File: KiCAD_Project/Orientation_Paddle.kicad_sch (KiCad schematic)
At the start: 54 parts, among them J1 NP_Conn_01x04_Relief, J2 1-0001205, J3 NP_Conn_01x03_Relief, J4 NP_Conn_01x02_Relief, J5 NP_Conn_01x02_Relief, J6 NP_Conn_01x04, J7 NP_Conn_01x04, J8 NP_Conn_01x02, U1 1-0001232, U2 1-0001471, U3 1-0000207, Y1 1-0000721

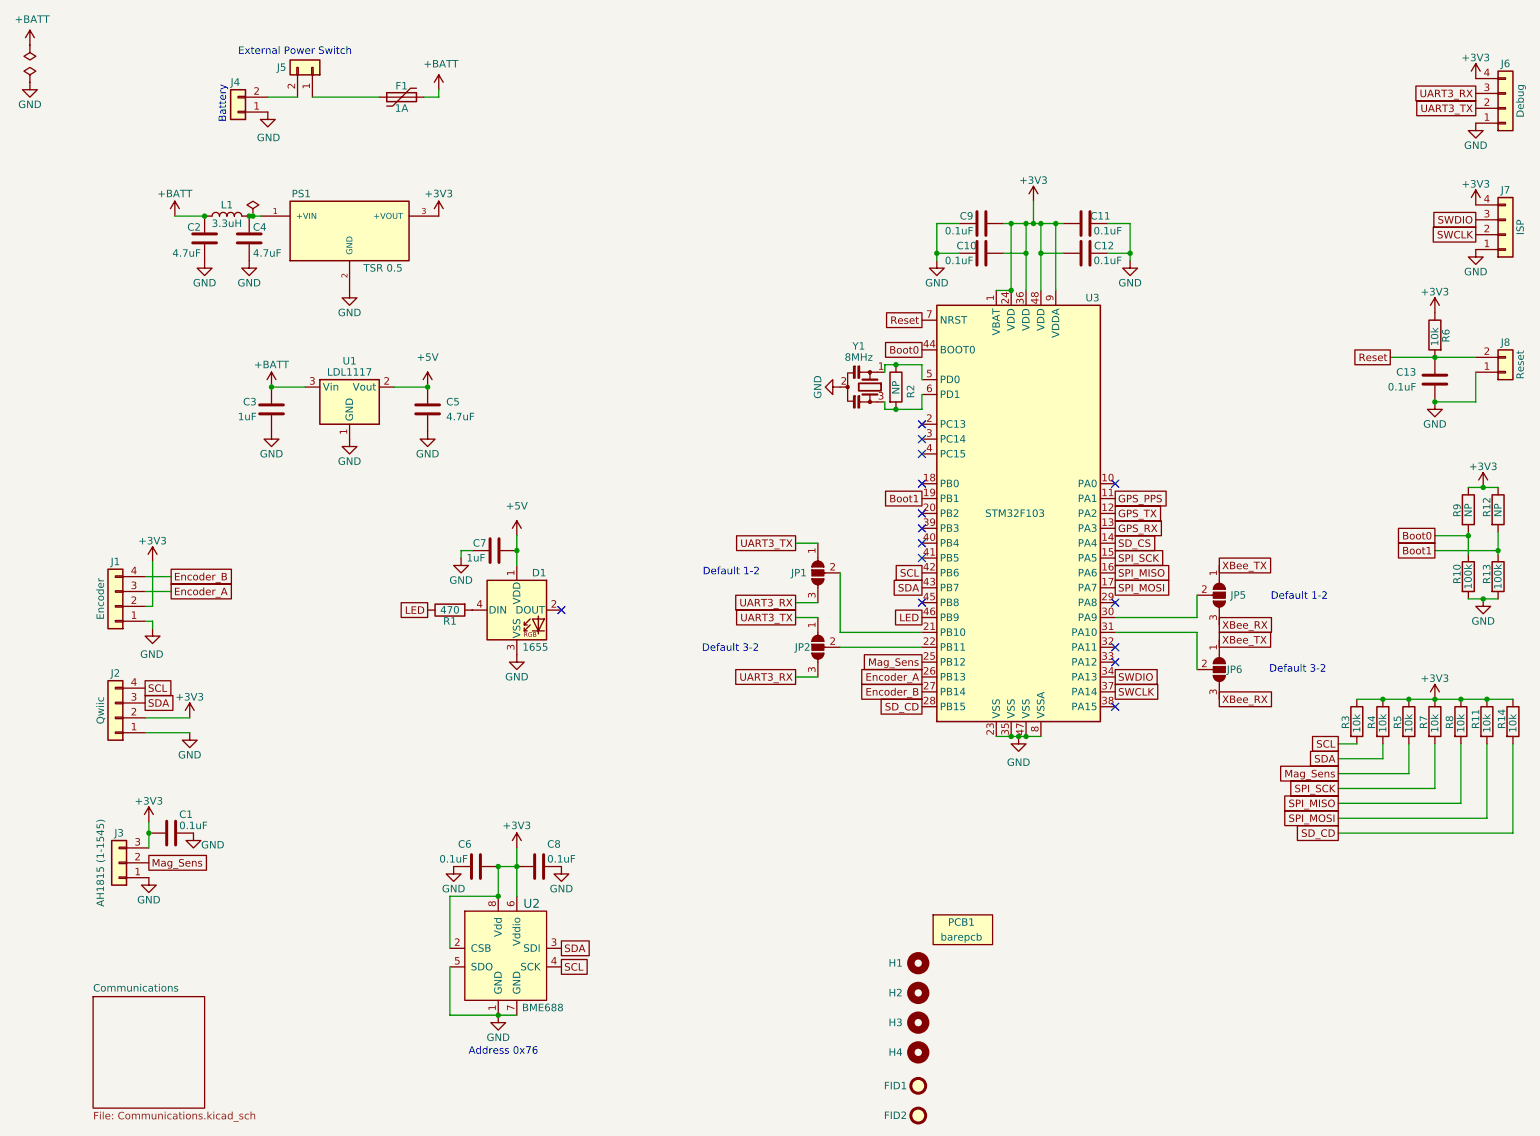
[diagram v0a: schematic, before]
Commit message: Rev 2.0 Changes: Fixed the following issues, - Issue #7 (Added RP Protection) - Issue #6 (Removed old encoder and sense connections) - Issue #5 (Solidified Serial connections by removing jumpers) - Issue #4 (Swapped GPS TX and RX) - Issue #3 (Removed old LED, add SMPL RGB LED) - Issue #2 (Labled ISCP Header) - Issue #1 (Changed DEBUG header to new SMPL DEBUG Connector) Other additions/changes: - Marked all XBEE Components as no pop - Updated board and rev numbers
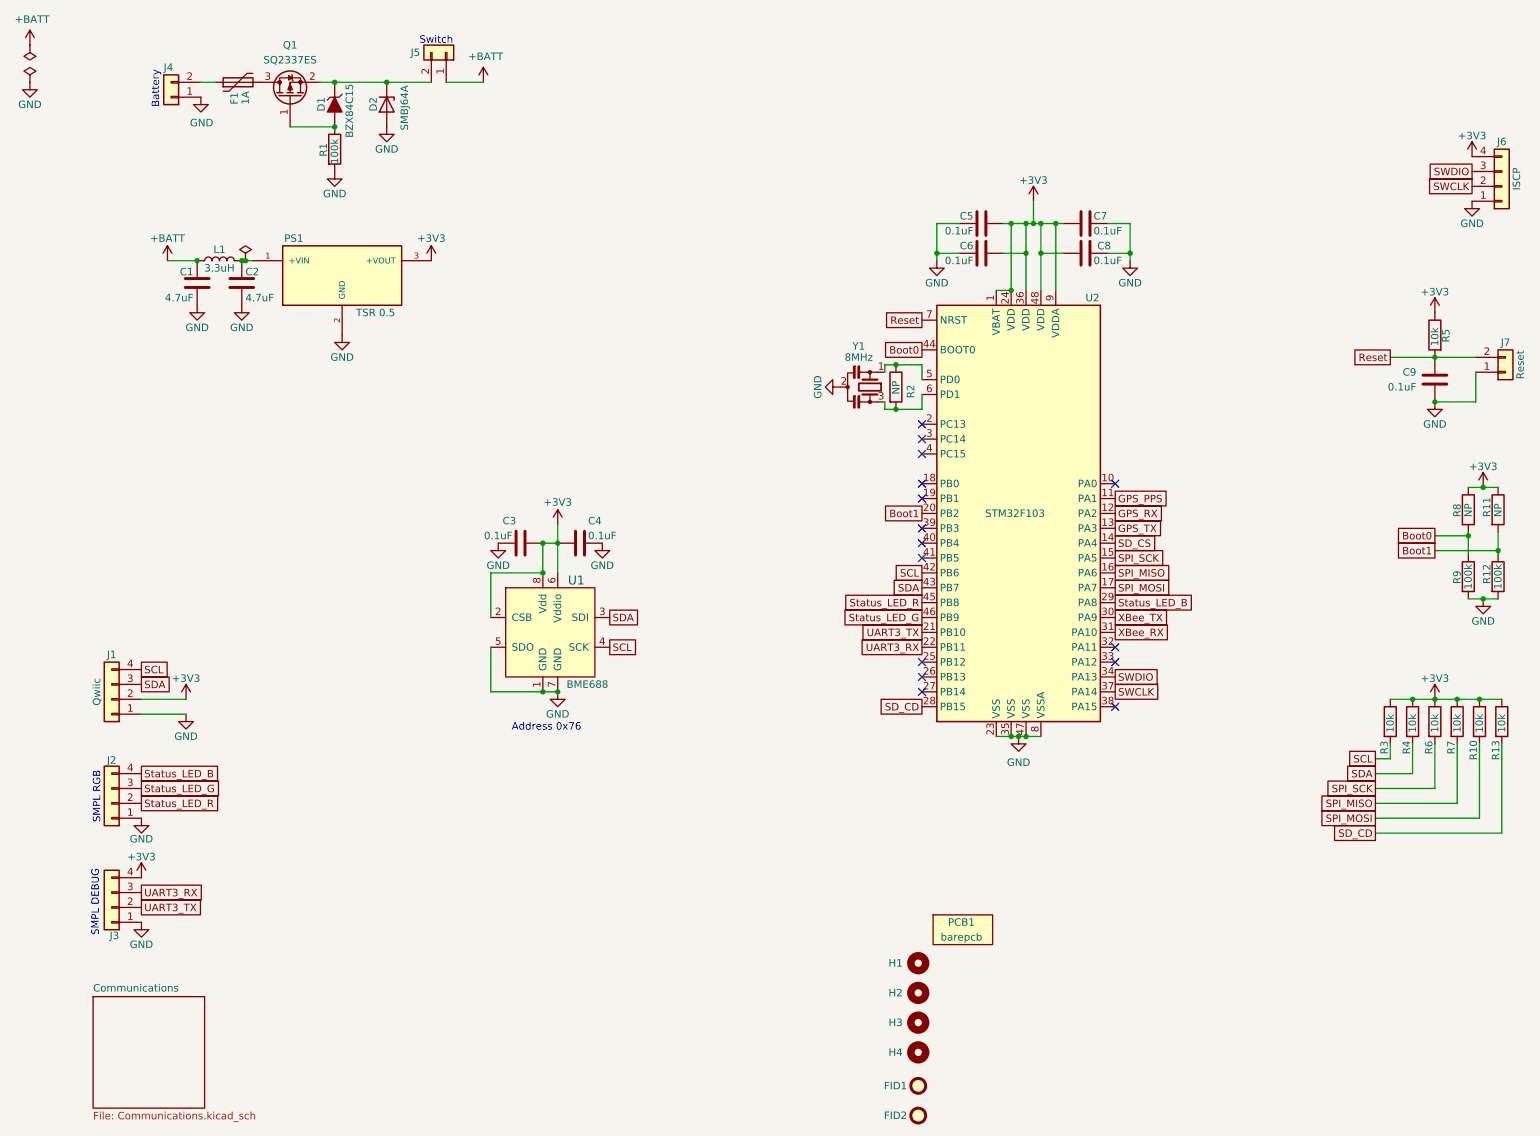
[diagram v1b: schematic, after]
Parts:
- removed C1, C6, C8: 1-0000007, capacitors_0603:1-0000007, symbol capacitors_0603:1-0000007
- removed C3, C7: 1-0000018, capacitors_0603:1-0000018, symbol capacitors_0603:1-0000018
- removed C5: 1-0000019, capacitors_0603:1-0000019, symbol capacitors_0603:1-0000019
- removed D1: 1-0000399, leds_other:1-0000399, symbol leds_other:1-0000399
- removed J1: NP_Conn_01x04_Relief, np_connectors:SolderWire_1x04_Relief, symbol np_connectors:NP_Conn_01x04_Relief
- removed J3: NP_Conn_01x03_Relief, np_connectors:SolderWire_1x03_Relief, symbol np_connectors:NP_Conn_01x03_Relief
- removed J6: NP_Conn_01x04, np_connectors:PinHeader_1x04_P2.54mm_Vertical, symbol np_connectors:NP_Conn_01x04
- removed JP1, JP2, JP5, JP6: SolderJumper_3_Open, Jumper:SolderJumper-3_P1.3mm_Open_RoundedPad1.0x1.5mm_NumberLabels, symbol Jumper:SolderJumper_3_Open
- removed R1: 1-0000679, resistors_0603:1-0000679, symbol resistors_0603:1-0000679
- removed R5: 1-0000010, resistors_0603:1-0000010, symbol resistors_0603:1-0000010
- removed U1: 1-0001232, regulators:1-0001232, symbol regulators:1-0001232
- removed U2: 1-0001471, sensors:1-0001471, symbol sensors:1-0001471
- added C3, C4: 1-0000007, capacitors_0603:1-0000007, symbol capacitors_0603:1-0000007
- added D1: 1-0001672, diodes:1-0001672, symbol diodes:1-0001672
- added D2: 1-0001537, diodes:1-0001537, symbol diodes:1-0001537
- added J2, J3: 1-0001156, connectors:1-0001156, symbol connectors:1-0001156
- added Q1: 1-0001670, mosfets:1-0001670, symbol mosfets:1-0001670
- added R1: 1-0000174, resistors_0603:1-0000174, symbol resistors_0603:1-0000174
- added U1: 1-0001471, sensors:1-0001471, symbol sensors:1-0001471
- J6: renamed from J7; PValue ISP -> ISCP
- PCB1: Internal Part Number 3-0000205 -> 3-0000267
- renumbered C2 to C1, C4 to C2, C9 to C5, C10 to C6, C11 to C7, C12 to C8, C13 to C9, J2 to J1, J8 to J7, R11 to R10, R12 to R11, R13 to R12, R14 to R13, R6 to R5, R7 to R6, R8 to R7, R9 to R8, R10 to R9, U3 to U2
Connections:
- net +3V3: now also C3.2, C4.1, J3.4 (Pin_4), U1.2 (CSB), U1.6 (Vddio), U1.8 (Vdd)
- net +BATT: now also J5.1 (Pin_1); no longer F1.2
- net Boot1: now also U2.20 (PB2); no longer U2.19 (PB1)
- net GND: now also C3.1, C4.2, D2.2 (A), J2.1 (Pin_1), J3.1 (Pin_1), R1.2, U1.1 (GND), U1.5 (SDO), U1.7 (GND)
- net GPS_RX: now also U2.12 (PA2); no longer U2.13 (PA3)
- net GPS_TX: now also U2.13 (PA3); no longer U2.12 (PA2)
- net SCL: now also U1.4 (SCK)
- net SDA: now also U1.3 (SDI)
- net UART3_RX: now also U2.22 (PB11), J3.3 (Pin_3)
- net UART3_TX: now also U2.21 (PB10), J3.2 (Pin_2)
- net XBee_RX: now also U2.31 (PA10)
- net XBee_TX: now also U2.30 (PA9)
- net at F1.1: now also J4.2 (Pin_2); no longer J5.1 (Pin_1)
- net Status_LED_B: now reaches U2.29 (PA8)
- net Status_LED_B: now also J2.4 (Pin_4)
- net Status_LED_R: now reaches U2.45 (PB8)
- net Status_LED_R: now also J2.2 (Pin_2)
- net at J5.2 (Pin_2): now also D1.3 (K), D2.1 (K), Q1.2 (S); no longer J4.2 (Pin_2)
- net Encoder_A: no longer names the net of U2.26 (PB13)
- net Encoder_B: no longer names the net of U2.27 (PB14)
- net LED renamed Status_LED_G
- net Status_LED_G: now also J2.3 (Pin_3)
- net Mag_Sens: no longer names the net of U2.25 (PB12)
- new net: F1.2, Q1.3 (D)
- new net: D1.1 (A), Q1.1 (G), R1.1
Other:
- note added: "SMPL DEBUG"
- note added: "SMPL RGB"
- note added: "Switch"
- note removed: "Default 1-2"
- note removed: "Default 3-2"
- note removed: "External Power Switch"
- moved on the sheet: C1, C2, J1, J4, J5, J6, L1, PS1, R10, R13, R3, R4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

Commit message: Make Rev 2.0 production files
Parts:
- C3, C4, U1: Populated 1 -> 0
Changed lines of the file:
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@@
 			"AAAAAAAAAAAAAAAAAAEAAAAmAAAmll+CACDQHh1QAgAAgO2YiVACAAAAAAAAAAAAAAAAAAABAAAA"
 			"AAAAAAAAAAAAAAAAAAAAAAAAAAAAAAAAAAAAAAAAAAAAAAAAAQAAAAAAAAAAAAAAAAAAAAAAAAAA"
+			"AAAAAAAAAFgBAAAAFAQAYgAAAAAAAAAyAQAA5QAAAAAAAAAAAAAAgzl9DQIAAAAAAAAAAAAAAAAA"
+			"AAAAAAAAVgEAAAAcBAA/AAAAAAAAABYBAAAvAAAAAAAAAAAAAADgYncNAgAAAAAAAAAAAAAAAAAA"
+			"AAAAAABQAQAAABQEAAYAAAAAAAAA//////////8AAAAAAAAAALAkfg0CAAAAAAAAAAAAAAAAAAAA"
+			"AAAAAGcBAAAAFAQAfAAAAAAAAAD//////////wAAAAAAAAAAgBz0AwBgAAAAAAAAAAAAAAAAAAAA"
+			"AAAAZgEAAAAUAgB9AAAAAAAAADsBAADNAAAAAAAAAAAAAADCH34NAgAAAAAAAAAAAAAAAAAAAAAA"
+			"AABlAQAAABQEAEUAAAAAAAAA/////wwBAAAAAAAAAAAAAD1Whg0CAAAAAAAAAAAAAAAAAAAAAAAA"
+			"AGIBAAAAFAQAIgAAAAAAAAD/////EQEAAAAAAAAAAAAA4GJ3DQIAAAAAAAAAAAAAAAAAAAAAAAAA"
+			"YQEAAAAUBAAGAAAAAAAAAP////8AAQAAAAAAAAAAAADgYncNAgAAAAAAAAAAAAAAAAAAAAAAAABg"
+			"AQAAABQEAAUAAAAAAAAAKgEAABoBAAAAAAAAAAAAAPxvew0CAAAAAAAAAAAAAAAAAAAAAAAAAGMB"
+			"AAAAHAQALQAAAAAAAAA8AQAAygAAAAAAAAAAAAAAwh9+DQIAAAAAAAAAAAAAAAAAAAAAAAAAZAEA"
+			"AAAUBABEAAAAAAAAABgBAAABAQAAAAAAAAAAAAD8b3sNAgAAAAAAAAAAAAAAAAAAAAAAAABdAQAA"
+			"ABwEAC0AAAAAAAAA//////////8AAAAAAAAAAGFXhg0CAAAAAAAAAAAAAAAAAAAAAAAAAHABAAAA"
+			"FAQAcwAAAAAAAAD//////////wAAAAAAAAAA/lWGDQIAAAAAAAAAAAAAAAAAAAAAAAAAbwEAAAAU"
+			"BAB0AAAAAAAAAP//////////AAAAAAAAAAClX4YNAgAAAAAAAAAAAAAAAAAAAAAAAABuAQAAABQE"
+			"AHUAAAAAAAAA//////////8AAAAAAAAAAGtfhg0CAAAAAAAAAAAAAAAAAAAAAAAAAG0BAAAAFAQA"
+			"dgAAAAAAAAD//////////wAAAAAAAAAAFVmGDQIAAAAAAAAAAAAAAAAAAAAAAAAAbAEAAAAUBAB3"
+			"AAAAAAAAAP//////////AAAAAAAAAADVWIYNAgAAAAAAAAAAAAAAAAAAAAAAAABrAQAAABQEAHgA"
+			"AAAAAAAA//////////8AAAAAAAAAALFYhg0CAAAAAAAAAAAAAAAAAAAAAAAAAGoBAAAAFAQAeQAA"
+			"AAAAAAD//wAAAAAAAAAAAAAAAAAAAAAAAAAAAAAAAAAAAAAAAAAAAAAAAAAAAAAAAAAAAAAAAAAA"
+			"AAAAAAAAAAAAAAAAAAAAAAAAAAAAAAAAAAAAAAAAAAAAAAAAAAAAAAAAAAAAAAAAAAAAAAAAAAAA"
+			"AAAAAAAAAAAAAAAAAAAAAAAAAAAAAAAAAAAAAAAAAAAAAAAAAAAAAAAAAE8UYD7oAAAAALCyNwEA"
+			"AABoCQAAAAAAAAAAAAAAAAAAAAAAAAAAAAAAAAAAAAAAAAAAAAAAAAAAAAAAAAAAAAAAAAAAAAAA"
+			"AAAAAAAAAAAAAAAAAAAAAAAAAAAAAAAAAAAAAAAAAAAAAAAAAAAAAAAAAAAAAAAAAAAAAAAAAAAA"
+			"AAAAAAAAAAAAAAAAAAAAAAAAAAAAAAAAAAAAAAAAAAAAAAAAAAAAAAAAAAAAAAAAAAAAAAAAAAAA"
+			"AAAAAAAAAAAAAAAAAAAAAAAAAAAAAAAAAAAAAAAAAAAAAAAAAAAAAAAAAAAAAAAAAAAAAAAAAAAA"
+			"AAAAAAAA/4J+gv+CfoL/gn6C/4J+gv+CfoL/gn6C/4J+gv+CfoL/gn6C/4J+gv+CfoL/gn6C/4J+"
+			"gv+CfoL/gn6C/4J+ggAAAAAAAAAAAAAAAAAAAAAAAAAAAAAAAAAAAAAAAAAA/4J+gv+CfoL/gn6C"
+			"/4J+gv+CfoL/gn6C/4J+gv+CfoL/gn6C/4J+gv+CfoL/gn6C/4J+gv+CfoL/gn6C/4J+ggAAAAAA"
+			"AAAAAAAAAAAAAAAAAAAAAAAAAAAAAAAAAAAA/4J+gv+CfoL/gn6C/4J+gv+CfoL/gn6C/4J+gv+C"
+			"foL/gn6C/4J+gv+CfoL/gn6C/4J+gv+CfoL/gn6C/4J+ggAAAAAAAAAAAAAAAAAAAAAAAAAAAAAA"
+			"AAAAAAAAAAAAAAAAAAAAAAAAAAAAAAAAAAAAAAAAAAAA/4J+gv+CfoL/gn6C/4J+ggAAAAAAAAAA"
+			"AAAAAAAAAAAAAAAAAAAAAAAAAAAAAAAAAAAAAAAAAAAAAAAAAAAAAAAAAAAAAAAAAAAAAAAAAAAA"
+			"AAAAAAAAAAAAAAAAAAAA/4J+gv+CfoL/gn6C/4J+ggAAAAAAAAAAAAAAAAAAAAAAAAAAAAAAAAAA"
+			"AAAAAAAAAAAAAAAAAAAAAAAAAAAAAAAAAAAAAAAAAAAAAAAAAAAAAAAAAAAAAAAAAAAAAAAA/4J+"
+			"gv+CfoL/gn6C/4J+ggAAAAAAAAAAAAAAAAAAAAAAAAAAAAAAAAAAAAAAAAAAAAAAAAAAAAAAAAAA"
+			"AAAAAAAAAAAAAAAAAAAAAAAAAAAAAAAAAAAAAAAAAAAAAAAA/4J+gv+CfoL/gn6C/4J+ggAAAAAA"
 			"AAAAAAAAAA=="
 		)
@@
 			)
 		)
-		(property "Populated" "1"
+		(property "Populated" "0"
 			(at 99.06 102.87 0)
 			(effects
@@
 			)
 		)
-		(property "Populated" "1"
+		(property "Populated" "0"
 			(at 93.98 118.11 0)
 			(effects
@@
 			)
 		)
-		(property "Populated" "1"
+		(property "Populated" "0"
 			(at 88.9 102.87 0)
 			(effects

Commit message: Fixed Issues #9, Issue #10 (Rev2.1)
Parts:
- PCB1: Internal Part Number 3-0000267 -> 3-0000273
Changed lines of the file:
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@@
 	(title_block
 		(title "Orientation Paddle")
-		(date "2025-06-03")
-		(rev "2.0.0")
+		(date "2025-07-03")
+		(rev "2.1.0")
 		(company "Leeman Geophysical LLC")
 		(comment 1 "(479) 373-3736")
@@
 			"gv+CfoL/gn6C/4J+ggAAAAAAAAAAAAAAAAAAAAAAAAAAAAAAAAAAAAAAAAAAAAAAAAAAAAAAAAAA"
 			"AAAAAAAAAAAAAAAAAAAAAAAAAAAAAAAAAAAAAAAAAAAAAAAA/4J+gv+CfoL/gn6C/4J+ggAAAAAA"
-			"AAAAAAAAAA=="
+			"AAAAAAAAAP//////////////////////////////////////////////////////////////////"
+			"////////////////////////////////////////////////////////////////////////////"
+			"////////////////////////////////////////////////////////////////////////////"
+			"////////////////////////////////////////////////////////////////////////////"
+			"////////////////////////////////////////////////////////////////////////////"
+			"////////////////////////////////////////////////////////////////////////////"
+			"////////////////////////////////////////////////////////////////////////////"
+			"////////////////////////////////////////////////////////////////////////////"
+			"////////////////////////////////////////////////////////////////////////////"
+			"////////////////////////////////////////////////////////////////////////////"
+			"////////////////////////////////////////////////////////////////////////////"
+			"////////////////////////////////////////////////////////////////////////////"
+			"////////////////////////////////////////////////////////////////////////////"
+			"////////////////////////////////////////////////////////////////////////////"
+			"////////////////////////////////////////////////////////////////////////////"
+			"////////////////////////////////////////////////////////////////////////////"
+			"////////////////////////////////////////////////////////////////////////////"
+			"////////////////////////////////////////////////////////////////////////////"
+			"/////////wAAAAAAAAAAAAAAAAAAAAAAAAAAAAAAAAAAAAAAAAAAAAAAAAAAAAAAAAAAAAAAAAAA"
+			"AAAAAAAAAAAAAAAAAAAAAAAAAAAAAAAAAAAAAAAAAAAAAAAAAAAAAAAAAAAAAAAAAAAAAAAAAAAA"
+			"AAAAAAAAAAAAAAAAAAAAAAAAAAAAAAAAAAAAAAAAAAAAAAAAAAAAAAAAAAAAAAAAAAAAAAAAAAAA"
+			"AAAAAAAAAAAAAAAAAAAAAAAAAAAAAAAAAAAAAAAAAAAAAAAAAAAAAAAAAAAAAAAAAAAAAAAAAAAA"
+			"AAAAAAAAAAAAAAAAAAAAAAAAAAAAAAAAAAAAAAAAAAAAAAAAAAAAAAAAAAAAAAAAAAAAAAAAAAAA"
+			"AAAAAAAAAAAAAAAAAAAAAAAAAAAAAAAAAAAAAAAAAAAAAAAAAAAAAAAAAAAAAAAAAAAAAAAAAAAA"
+			"AAAAAAAAAAAAAAAAAAAAAAAAAAAAAAAAAAAAAAAAAAAAAAAAAAAAAAAAAAAAAAAAAAAAAAAAAAAA"
+			"AAAAAAAAAAAAAAAAAAAAAAAAAAAAAAAAAAAAAAAAAAAAAAAAAAAAAAAAAAAAAAAAAAAAAAAAAAAA"
+			"AAAAAAAAAAAAAAAAAAAAAAAAAAAAAAAAAAAAAAAAAAAAAAAAAAAAAAAAAAAAAAAAAAAAAAAAAAAA"
+			"AAAAAAAAAAAAAAAAAAAAAAAAAAAAAAAAAAAAAAAAAAAAAAAAAAAAAAAAAAAAAAAAAAAAAAAAAAAA"
+			"AAAAAAAAAAAAAAAAAAAAAAAAAAAAAAAAAAAAAAAAAAAAAAAAAAAAAAAAAAAAAAAAAAAAAAAAAAAA"
+			"AAAAAAAAAAAAAAAAAAAAAAAAAAAAAAAAAAAAAAAAAAAAAAAAAAAAAAAAAAAAAAAAAAAAAAAAAAAA"
+			"AAAAAAAAAAAAAAAAAAAAAAAAAAAAAAAAAAAAAAAAAAAAAAAAAAAAAAAAAAAAAAAAAAAAAAAAAAAA"
+			"AAAAAAAAAAAAAAAAAAAAAAAAAAAAAAAAAAAAAAAAAAAAAAAAAAAAAAAAAAAAAAAAAAAAAAAAAAAA"
+			"AAAAAAAAAAAAAAAAAAAAAAAAAAAAAAAAAAAAAAAAAAAAAAAAAAAAAAAAAAAAAAAAAAAAAAAAAAAA"
+			"AAAAAAAAAAAAAAAAAAAAAAAAAAAAAAAAAAAAAAAAAAAAAAAAAAAAAAAAAAAAAAAAAAAAAAAAAAAA"
+			"AAAAAAAAAAAAAAAAAAAAAAAAAAAAAAAAAAAAAAAAAAAAAAAAAAAAAAAAAAAAAAAAAAAAAAAAAAAA"
+			"AAAAAAAAAAAAAAAAAAAAAAAAAAAAAAAAAAAAAAAAAAAAAAAAAAAAAAAAAAAAAAAAAAAAAAAAAAAA"
+			"AAAAAAAAAGRlcmVkQnl0ZUFkZHJlc3NCdWZmZXJSYXN0ZXJpemVyT3JkZXJlZFZpZXdzTWluTk9T"
+			"UHVzaENvbnN0YW50U2l6ZWlubGluZVByb2dyYW1TY29wZU9mZnNldHNzaGFkZXJEYXRhbnVtUmVw"
+			"bGljYXNVUkJJbmZvaGFzNjRCVmVydGV4SGVhZGVySW5wdXRoYXM2NEJWZXJ0ZXhIZWFkZXJPdXRw"
+			"dXRoYXNWZXJ0ZXhIZWFkZXJVc2VCaW5kbGVzc0ltYWdlZW5hYmxlUmFuZ2VSZWR1Y2VkaXNhYmxl"
+			"TmV3VHJpZ0Z1bmNSYW5nZVJlZHVjdGlvbmVuYWJsZUZSZW1Ub1NSZW1PcHRlbmFibGVTYW1wbGVw"
+			"dHJUb0xkbXNwdHJTYW1wbGUwV2FGb3JjZVNJTUQzMk1pY3JvcG9seVJhc3Rlcml6ZVdhRW5hYmxl"
+			"RmFzdGVzdEZvckFsbFdhdmVJbnRyaW5zaWNzQ1NXYUVuYWJsZUZhc3Rlc3RGb3JBbGxXYXZlSW50"
+			"cmluc2ljc1BTYWxsb3dNYXRjaE1hZE9wdGltaXphdGlvbmZvclZTZGlzYWJsZU1hdGNoTWFkT3B0"
+			"aW1pemF0aW9uRm9yQ1NkaXNhYmxlTWVtT3B0Zm9yTmVnYXRpdmVPZmZzZXRMb2Fkc2VuYWJsZVRo"
+			"cmVlV2F5TG9hZFNwaWx0T3B0c3RhdGVmdWxSZXNvdXJjZXNOb3RBbGlhc2VkZGlzYWJsZU1peE1v"
+			"ZGVnZW5lcmljQWNjZXNzZXNSZXNvbHZlZGRpc2FibGVTZXBhcmF0ZVNwaWxsUHZ0U2NyYXRjaFNw"
+			"YWNlZGlzYWJsZVNlcGFyYXRlU2NyYXRjaFdBUHJpdmF0ZU1lbW9yeVBlckZHbV9PcHRzVG9EaXNh"
+			"YmxlY2FwYWJpbGl0aWVzZ2xvYmFsVmFyaWFibGVEZWNvcmF0aW9uc0lOVEVMbV9TaGFkZXJSZXNv"
+			"dXJjZVZpZXdNY3NNYXNrbV9TaGFkZXJSZXNvdXJjZVZpZXdNY3NNYXNrVmVjWzBdbV9TaGFkZXJS"
+			"ZXNvdXJjZVZpZXdNY3NNYXNrVmVjWzFdY29tcHV0ZWREZXB0aE1vZGVpc0hEQ0Zhc3RDbGVhclNo"
+			"YWRlcmYyBAAAAAAAMIIAFSMIQDWCAFgjCNc2gnBxIwjANYIAYCMIadCNIKiBN4LQaCMIQDaDEOTK"
+			"DEGuzBDoygyDQC7lMoMwLuYyg4Ar5zKDQOzKDIKxKzMIx67MICC7MoOQ7MoMgsIrMwjLrswgMLwy"
+			"g9DkygyC0yszCI+vzCBAvjKDEOXKDIKUKzMI067MIFC7MoNQ7coMgrUrMwjXrswgYLwyg5DtygyC"
+			"tiszCBuvzA=="
 		)
 	)
@@
 			)
 		)
-		(property "Internal Part Number" "3-0000267"
+		(property "Internal Part Number" "3-0000273"
 			(at 164.465 168.91 0)
 			(effects
